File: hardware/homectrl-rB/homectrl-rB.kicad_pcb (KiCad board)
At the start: 4 copper layers, 134 x 86.2 mm, 116 parts, among them J1 Barrel_Jack, J2 USB_C_Female_USB2_Small, J3 SMS-CONN-0, J4 SMS-CONN-1, J5 ALS_CONN, J6 PUMP0-CONN, J7 PUMP1-CONN, J8 STEP-CONN, Q1 DMP6023LE-13, Q2 IRLZ44N, Q3 IRLZ44N, SW1 SW_RESET, SW2 SW_BOOT, U1 ESP32-S3-WROOM-1, U2 TPS5405DR, U3 ID_LM66100DCKR, U4 ID_LM66100DCKR, U5 ADS1115IDGS, U6 SI2301, U7 SI2301, U8 TMC2209

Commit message: routing work
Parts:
- moved R13 7.02 mm to (116.8, 93.9), turned to 90 degrees
- moved R12 4.02 mm to (114.5, 93.9)
- moved VR1 3.32 mm to (103.0, 68.5)
- moved C10 3.32 mm to (96.3, 66.0)
- moved C7 3.32 mm to (96.3, 64.5)
- moved R10 2.16 mm to (137.0, 118.7), turned to 90 degrees
- moved C27 1.94 mm to (148.5, 114.8)
- moved R14 1.50 mm to (105.0, 87.8), turned to -90 degrees
- moved C36 1.29 mm to (98.8, 104.1)
- moved D7 1.29 mm to (100.7, 99.8)
- moved C37 1.29 mm to (97.4, 105.9)
- moved R30 1.29 mm to (97.2, 97.3)
- moved R9 1.19 mm to (142.2, 116.5)
- moved C17 1.10 mm to (88.4, 96.6)
- moved C18 1.10 mm to (89.9, 96.6)
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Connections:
- U1 pad 38: S3-SDA -> S3-SCL
- U1 pad 39: S3-SCL -> S3-SDA
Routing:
- net +3V3: track 0.00 -> 203.8 mm, vias 0 -> 6
- net GND: track 0.00 -> 166.8 mm, vias 0 -> 83
- net +12V: track 0.00 -> 114.0 mm, vias 0 -> 3
- net S3-SCL: track 0.00 -> 80.0 mm, vias 0 -> 2
- net S3-SDA: track 0.00 -> 77.7 mm
- net PGATE-1: track 0.00 -> 32.7 mm
- net USB_D+: track 0.00 -> 26.4 mm
- net PGATE-0: track 0.00 -> 24.9 mm
- net +5V: track 0.00 -> 24.5 mm
- net USB_D-: track 0.00 -> 22.1 mm
- net Net-(D2-A1): track 0.00 -> 19.5 mm
- net Net-(D3-A): track 0.00 -> 17.0 mm
- net 2B: track 0.00 -> 16.8 mm
- net EN: track 0.00 -> 15.0 mm
- net Net-(D1-K): track 0.26 -> 15.3 mm
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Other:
- outline, holes or cut-outs redrawn

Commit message: more routing work
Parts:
- moved R9 2.85 mm to (140.5, 118.8), turned to 90 degrees
- moved C29 1.32 mm to (141.8, 106.5)
- moved C19 0.55 mm to (114.2, 91.1)
- moved C20 0.29 mm to (112.5, 91.2)
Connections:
- R7 pad 1: /ESP32-S3 Breakout/GPIO_05 -> /ESP32-S3 Breakout/GPIO_42
- R8 pad 1: /ESP32-S3 Breakout/GPIO_06 -> /ESP32-S3 Breakout/GPIO_41
- U1 pad 10: S3-TX -> PGATE-0
- U1 pad 11: S3-RX -> PGATE-1
- U1 pad 17: PGATE-0 -> /ESP32-S3 Breakout/GPIO_09
- U1 pad 18: PGATE-1 -> /ESP32-S3 Breakout/GPIO_10
- U1 pad 19: STEP -> /ESP32-S3 Breakout/GPIO_11
- U1 pad 20: DIR -> /ESP32-S3 Breakout/GPIO_12
- U1 pad 21: ENN -> /ESP32-S3 Breakout/GPIO_13
- U1 pad 34: unconnected-(U1-IO41-Pad34) -> /ESP32-S3 Breakout/GPIO_41
- U1 pad 35: unconnected-(U1-IO42-Pad35) -> /ESP32-S3 Breakout/GPIO_42
- U1 pad 4: ADC-RDY -> unconnected-(U1-IO4-Pad4)
- U1 pad 5: /ESP32-S3 Breakout/GPIO_05 -> STEP
- U1 pad 6: /ESP32-S3 Breakout/GPIO_06 -> DIR
- U1 pad 7: SGATE-0 -> S3-TX
- U1 pad 8: /ESP32-S3 Breakout/GPIO_15 -> S3-RX
- U1 pad 9: /ESP32-S3 Breakout/GPIO_16 -> ENN
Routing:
- net +3V3: track 203.8 -> 275.6 mm, vias 6 -> 9
- net +12V: track 114.0 -> 183.1 mm, vias 3 -> 5
- net SGATE-1: track 6.28 -> 35.8 mm, vias 2 -> 3
- net STEP: track 6.77 -> 35.4 mm, vias 2 -> 6
- net S3-RX: track 1.59 -> 30.1 mm, vias 1 -> 4
- net S3-TX: track 2.40 -> 30.1 mm, vias 0 -> 4
- net DIR: track 8.13 -> 34.1 mm, vias 2 -> 4
- net EN: track 15.0 -> 38.2 mm, vias 0 -> 2
- net ENN: track 0.00 -> 22.2 mm, vias 0 -> 4
- net SGATE-0: track 6.89 -> 26.8 mm, vias 2 -> 1
- net ADC-RDY: track 5.37 -> 24.4 mm
- net /ESP32-S3 Breakout/GPIO_14: track 1.68 -> 18.9 mm
- net AOUT-0: track 8.03 -> 22.8 mm, vias 1 -> 2
- net AOUT-1: track 9.49 -> 23.8 mm
- net +5V: track 24.5 -> 37.1 mm
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
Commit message: more more routing routing work work
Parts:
- U1: footprint ESP32-S3-WROOM-1-N16R2:XCVR_ESP32-S3-WROOM-1-N16R2 -> RF_Module:ESP32-S3-WROOM-1
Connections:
- Q1 pad 4: (no net) -> Net-(D2-A1)
- U1 pad 19: /ESP32-S3 Breakout/GPIO_11 -> ADC-RDY
- U1 pad 20: /ESP32-S3 Breakout/GPIO_12 -> SGATE-1
- U1 pad 21: /ESP32-S3 Breakout/GPIO_13 -> SGATE-0
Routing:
- net ADC-RDY: track 24.4 -> 46.6 mm, vias 1 -> 2
- net SGATE-1: track 35.8 -> 55.0 mm, vias 3 -> 4
- net SGATE-0: track 26.8 -> 42.9 mm, vias 1 -> 2
- net /ESP32-S3 Breakout/GPIO_14: track 18.9 -> 31.9 mm, vias 1 -> 2
- net /ESP32-S3 Breakout/GPIO_12: track 2.34 -> 0.00 mm, vias 1 -> 0
- net /ESP32-S3 Breakout/GPIO_11: track 1.72 -> 0.00 mm, vias 1 -> 0
- net unconnected-(D7-DOUT-Pad2): track 0.00 -> 0.98 mm
- net GND: vias 85 -> 116

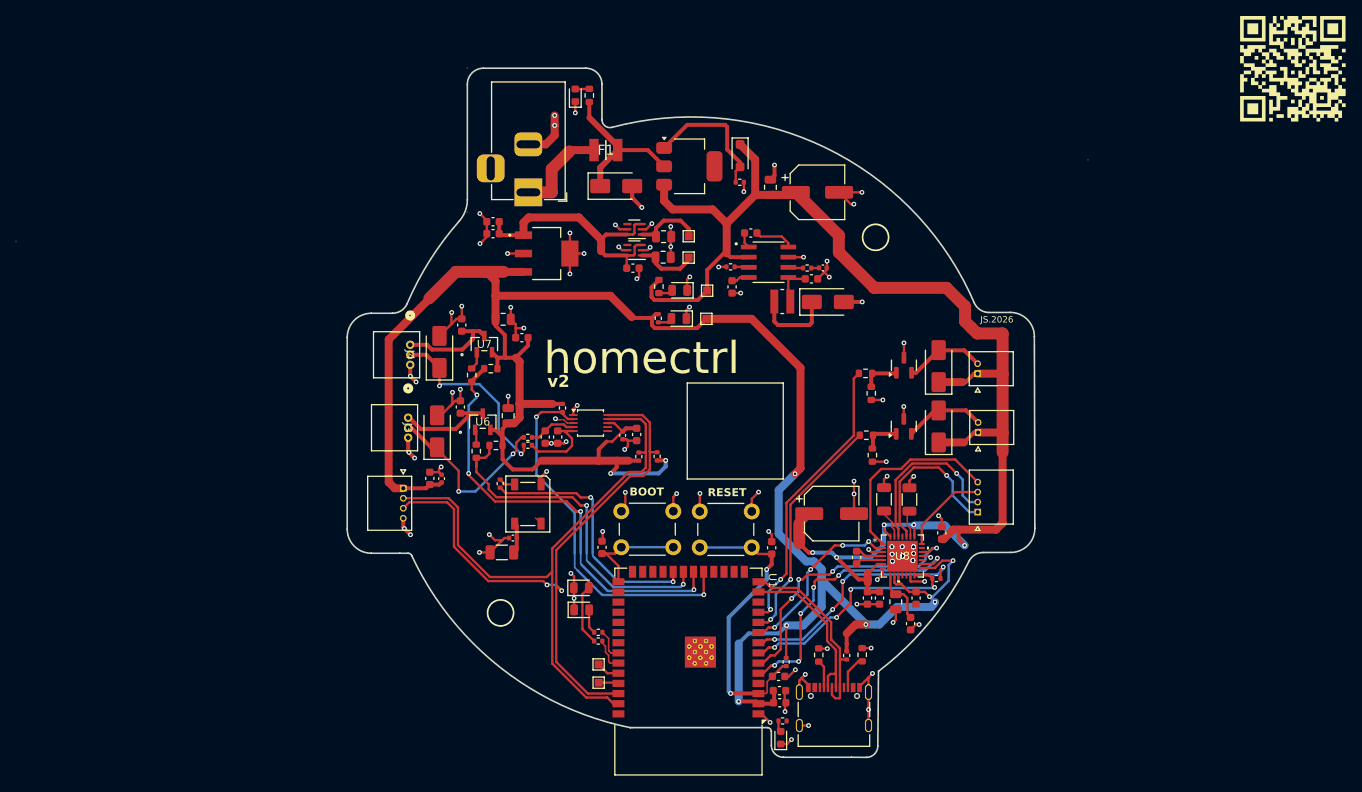
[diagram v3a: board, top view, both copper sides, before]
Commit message: silkscreen, review work
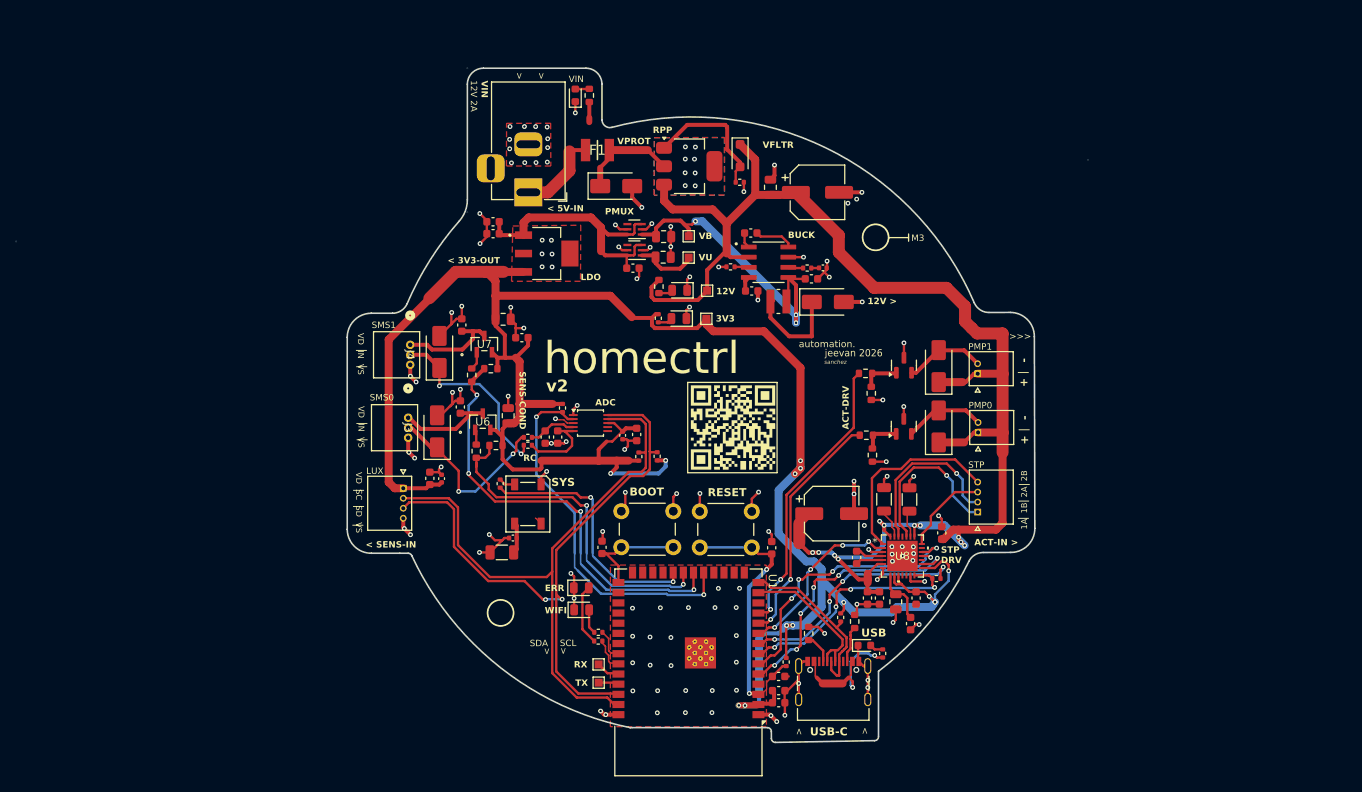
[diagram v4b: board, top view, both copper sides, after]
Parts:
- removed the G*** at (196.3, 45.4)
- added ?: , clipboard:d7d3f97e-8634-446f-a052-60447301ad40, B.Cu at (95.6, 113.4)
- added ?: , clipboard:d7d3f97e-8634-446f-a052-60447301ad40, B.Cu at (142.5, 66.5)
- added G***: LOGO, QR-CODE:qR, F.Cu at (126.3, 90.2)
- moved D14 15.6 mm to (142.7, 117.5), turned to 0 degrees
- moved R28 15.1 mm to (145.0, 118.5), turned to 90 degrees
- moved R9 4.81 mm to (139.8, 114.0)
- moved R11 4.26 mm to (141.5, 114.5)
- moved J2 3.26 mm to (138.8, 122.0)
- moved R10 2.97 mm to (135.8, 116.0)
- moved C5 2.51 mm to (128.6, 73.2), turned to 180 degrees
- moved F1 1.06 mm to (109.3, 55.6)
- moved L1 0.49 mm to (132.0, 74.5)
- moved C16 0.13 mm to (132.0, 124.7)
- moved C15 0.10 mm to (132.0, 123.2)
- moved U1 0.10 mm to (120.7, 120.9)
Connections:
- U1 pad 41: (no net) -> GND
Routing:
- net 5V-B: track 14.1 -> 40.8 mm, vias 0 -> 3
- net 5V-U: track 7.73 -> 26.1 mm, vias 0 -> 2
- net GND: track 175.2 -> 162.0 mm, vias 116 -> 123
- net +12V: track 183.1 -> 188.3 mm, vias 5 -> 11
- net Net-(D2-A1): track 19.5 -> 15.2 mm, vias 0 -> 14
- net EN: track 38.2 -> 34.5 mm
- net +5V: track 37.1 -> 39.9 mm
- net USB_D-: track 21.2 -> 18.5 mm
- net Net-(D1-K): track 15.3 -> 17.6 mm
- net USB_D+: track 24.1 -> 22.4 mm
- net S3-SCL: track 80.0 -> 81.4 mm
- net Net-(F1-Pad1): track 11.8 -> 10.8 mm
- net STEP: track 35.4 -> 34.4 mm
- net S3-SDA: track 77.7 -> 78.4 mm
- net PGATE-0: track 29.3 -> 29.9 mm
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- added copper zone on F.Cu, net GND
- added copper zone on B.Cu, net Net-(D2-A1)
- added copper zone on F.Cu, net Net-(D2-A1)
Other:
- board size 134 x 86.2 mm -> 134 x 84.3 mm
- board text added: "+ -"
- board text added: "12V"
- board text added: "12V 2A"
- board text added: "12V >"
- board text added: "1A 1B 2A 2B"
- board text added: "3V3"
- board text added: "<"
- board text added: "< 3V3-OUT"
- board text added: "< 5V-IN"
- board text added: "< SENS-IN"
- board text added: ">"
- board text added: ">>>"
- board text added: "ACT-DRV"
- board text added: "ACT-IN >"
- board text added: "ADC"
- board text added: "BUCK"
- board text added: "ERR"
- board text added: "LDO"
- board text added: "LUX"
- board text added: "M3"
- board text added: "PMP0"
- board text added: "PMP1"
- board text added: "PMUX"
- board text added: "RC"
- board text added: "REV B"
- board text added: "RPP"
- board text added: "RX"
- board text added: "SCL"
- board text added: "SDA"
- board text added: "SENS-COND"
- board text added: "SMS0"
- board text added: "SMS1"
- board text added: "STP"
- board text added: "STP DRV"
- board text added: "SYS"
- board text added: "TX"
- board text added: "USB"
- board text added: "USB-C"
- board text added: "VB"
- board text added: "VD IN VS"
- board text added: "VD SC SD VS"
- board text added: "VFLTR"
- board text added: "VIN"
- board text added: "VPROT"
- board text added: "VU"
- board text added: "WIFI"
- board text added: "automation."
- board text added: "jeevan 2026"
- board text added: "sanchez"
- board text added: "|"
- board text removed: "JS.2026"

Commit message: switch commit
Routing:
- net AOUT-0: track 22.8 -> 23.4 mm
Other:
- board text added: "PCB: 2L FR4, 1.6mm, HASL PWR: 12VDC, 2A"
- board text added: "designed in Toronto"
- board text added: "git"
- board text added: "homectrl v1.0"
- board text added: "jeevan sanchez | 2026.01.12"

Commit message: back silkscreen
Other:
- board text added: "*****"
- board text added: "- DC PUMP x2 - STEP"
- board text added: "- SMS x2 - LUX"
- board text added: "ACT-IN"
- board text added: "PCB: 2L FR4, 1.6mm, HASL PWR: 12VDC, 2A MCU: ESP32-S3"
- board text added: "SENS-IN"
- board text added: "USBC-IN"
- board text added: "WIFI | IoT ready"
- board text added: "home automation controller"
- board text removed: "PCB: 2L FR4, 1.6mm, HASL PWR: 12VDC, 2A"

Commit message: fix some text stuff
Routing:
- added copper zone on In1.Cu, net GND
- added copper zone on In2.Cu, net GND
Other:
- board text added: "- SMS x2 - ALS"
- board text added: "ALS"
- board text removed: "- SMS x2 - LUX"
- board text removed: "LUX"
- board text removed: "homectrl v1.0"

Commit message: getting there
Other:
- board text added: "PCB: 4L FR4, 1.6mm, HASL PWR: 12VDC, 2A MCU: ESP32-S3"
- board text removed: "PCB: 2L FR4, 1.6mm, HASL PWR: 12VDC, 2A MCU: ESP32-S3"
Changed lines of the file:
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@@
 		)
 		(property "Value" "2.2uF 10V"
-			(at 0 1.43 -90)
+			(at -0.02 1.49 -90)
 			(layer "F.Fab")
 			(effects
@@
 		)
 	)
-	(gr_text "PCB: 2L FR4, 1.6mm, HASL\n\nPWR: 12VDC, 2A \n\nMCU: ESP32-S3\n\n"
+	(gr_text "PCB: 4L FR4, 1.6mm, HASL\n\nPWR: 12VDC, 2A \n\nMCU: ESP32-S3\n\n"
 		(at 110.25 80 0)
 		(layer "B.SilkS")
@@
 			(justify left bottom mirror)
 		)
-		(render_cache "PCB: 2L FR4, 1.6mm, HASL\n\nPWR: 12VDC, 2A \n\nMCU: ESP32-S3\n\n"
+		(render_cache "PCB: 4L FR4, 1.6mm, HASL\n\nPWR: 12VDC, 2A \n\nMCU: ESP32-S3\n\n"
 			0
 			(polygon
@@
 			(polygon
 				(pts
-					(xy 106.246517 72.715501) (xy 106.835081 72.715501) (xy 106.835081 72.586992) (xy 106.800599 72.558398)
-					(xy 106.766051 72.529836) (xy 106.731437 72.501308) (xy 106.712178 72.485473) (xy 106.678169 72.456911)
-					(xy 106.645505 72.428448) (xy 106.614188 72.400084) (xy 106.597372 72.384368) (xy 106.564067 72.35266)
-					(xy 106.534218 72.323059) (xy 106.502963 72.290323) (xy 106.47279 72.255967) (xy 106.446602 72.221764)
-					(xy 106.443951 72.217868) (xy 106.422055 72.178228) (xy 106.408269 72.136642) (xy 106.402592 72.093109)
-					(xy 106.40243 72.084169) (xy 106.407704 72.04257) (xy 106.425488 72.004856) (xy 106.447065 71.981819)
-					(xy 106.485534 71.959301) (xy 106.529568 71.947789) (xy 106.571837 71.944865) (xy 106.616458 71.947572)
-					(xy 106.660201 71.954876) (xy 106.686851 71.961266) (xy 106.72904 71.974578) (xy 106.770543 71.991962)
-					(xy 106.807677 72.0113) (xy 106.81349 72.0113) (xy 106.81349 71.891511) (xy 106.771874 71.874747)
-					(xy 106.731761 71.862524) (xy 106.702836 71.855179) (xy 106.660034 71.846421) (xy 106.618042 71.840907)
-					(xy 106.572788 71.838587) (xy 106.568722 71.838571) (xy 106.520622 71.84079) (xy 106.476594 71.847446)
-					(xy 106.430375 71.860821) (xy 106.3897 71.880235) (xy 106.359248 71.901683) (xy 106.329641 71.931441)
-					(xy 106.304708 71.970704) (xy 106.289274 72.015573) (xy 106.28356 72.059432) (xy 106.283264 72.072751)
-					(xy 106.286046 72.116881) (xy 106.294394 72.158182) (xy 106.295928 72.163475) (xy 106.311394 72.204322)
-					(xy 106.332882 72.242988) (xy 106.357691 72.278178) (xy 106.384531 72.310602) (xy 106.386444 72.312744)
-					(xy 106.415691 72.344148) (xy 106.447402 72.37587) (xy 106.460767 72.388728) (xy 106.492271 72.418494)
-					(xy 106.524295 72.447792) (xy 106.556837 72.476623) (xy 106.589898 72.504988) (xy 106.622661 72.532599)
-					(xy 106.658186 72.562422) (xy 106.692298 72.59093) (xy 106.714255 72.609206) (xy 106.246517 72.609206)
+					(xy 106.884077 72.342017) (xy 106.884077 72.476338) (xy 106.467826 72.476338) (xy 106.467826 72.715501)
+					(xy 106.355718 72.715501) (xy 106.355718 72.476338) (xy 106.226795 72.476338) (xy 106.226795 72.38333)
+					(xy 106.355718 72.38333) (xy 106.467826 72.38333) (xy 106.804771 72.38333) (xy 106.467826 71.990746)
+					(xy 106.467826 72.38333) (xy 106.355718 72.38333) (xy 106.355718 71.851858) (xy 106.463258 71.851858)
 				)
 			)
@@
 		(hatch edge 0.5)
 		(priority 4)
-		(connect_pads yes
+		(connect_pads thru_hole_only
 			(clearance 0.5)
 		)
 		(min_thickness 0.25)
 		(filled_areas_thickness no)
-		(fill
+		(fill yes
 			(thermal_gap 0.5)
 			(thermal_bridge_width 0.5)
